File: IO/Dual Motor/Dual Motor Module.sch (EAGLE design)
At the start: 17 parts, among them U1 PCA9685, U2 DRV8837, U3 DRV8837, U7 TPS62142

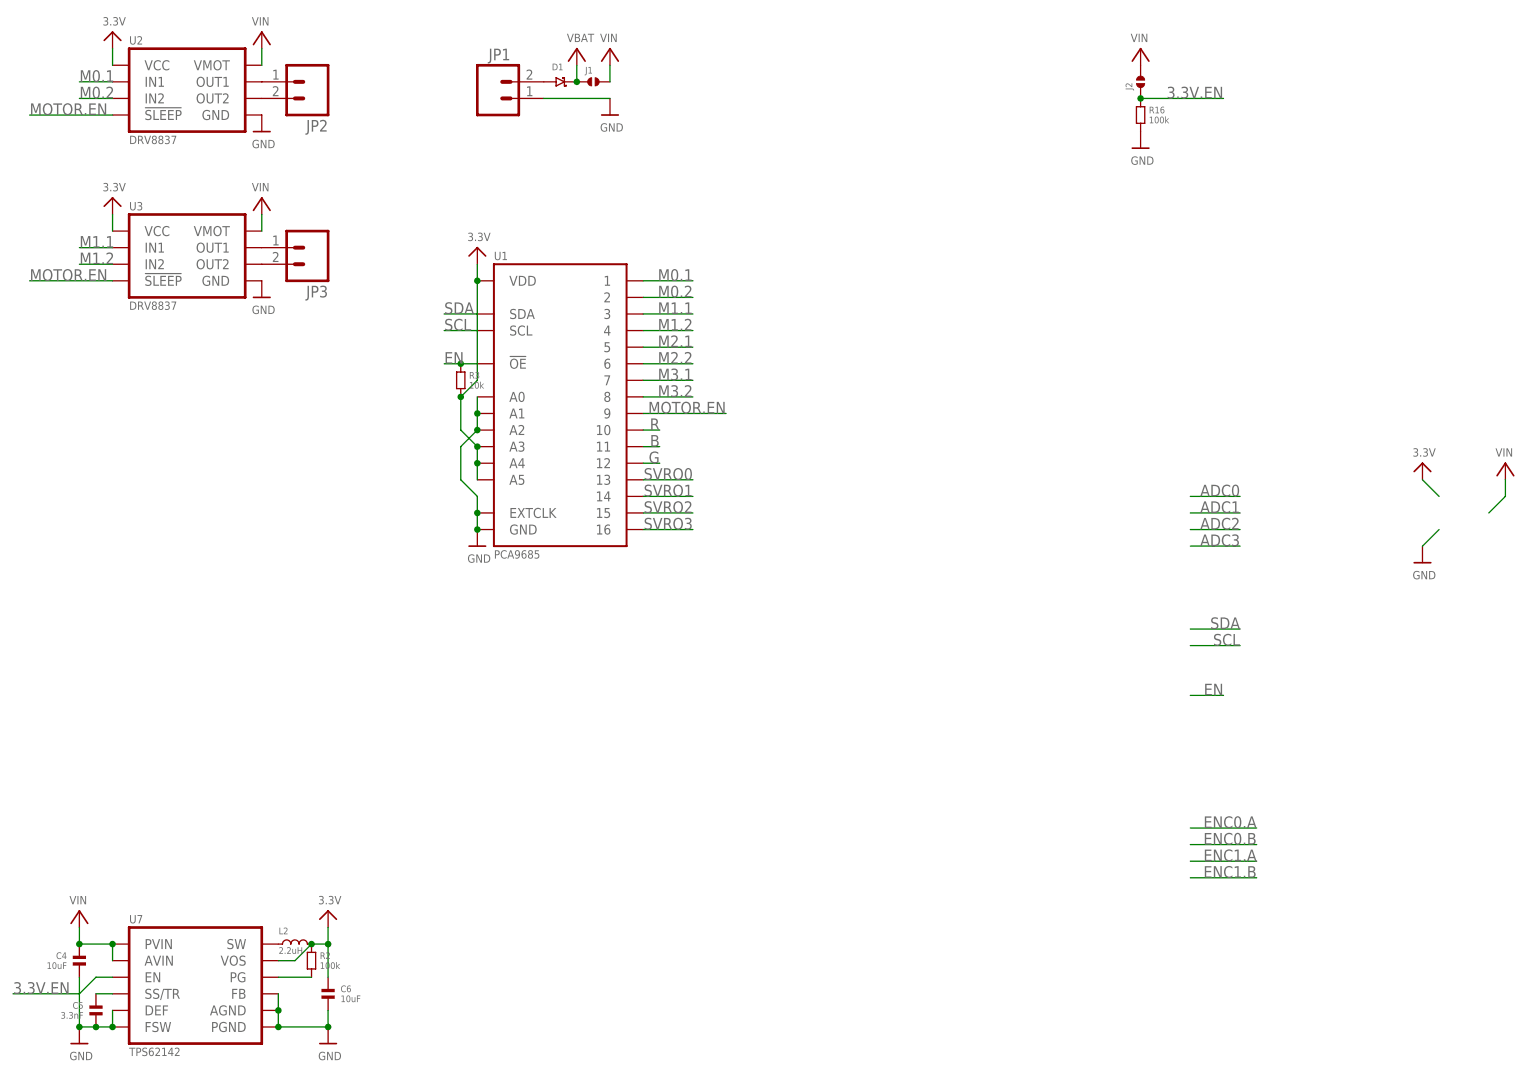
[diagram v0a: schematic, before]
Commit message: Created Dual Motor Module. Schematic complete, components laid out, routing still needed.
Signed-off-by: Cruz Monrreal II <Cruz.Monrreal@gmail.com>
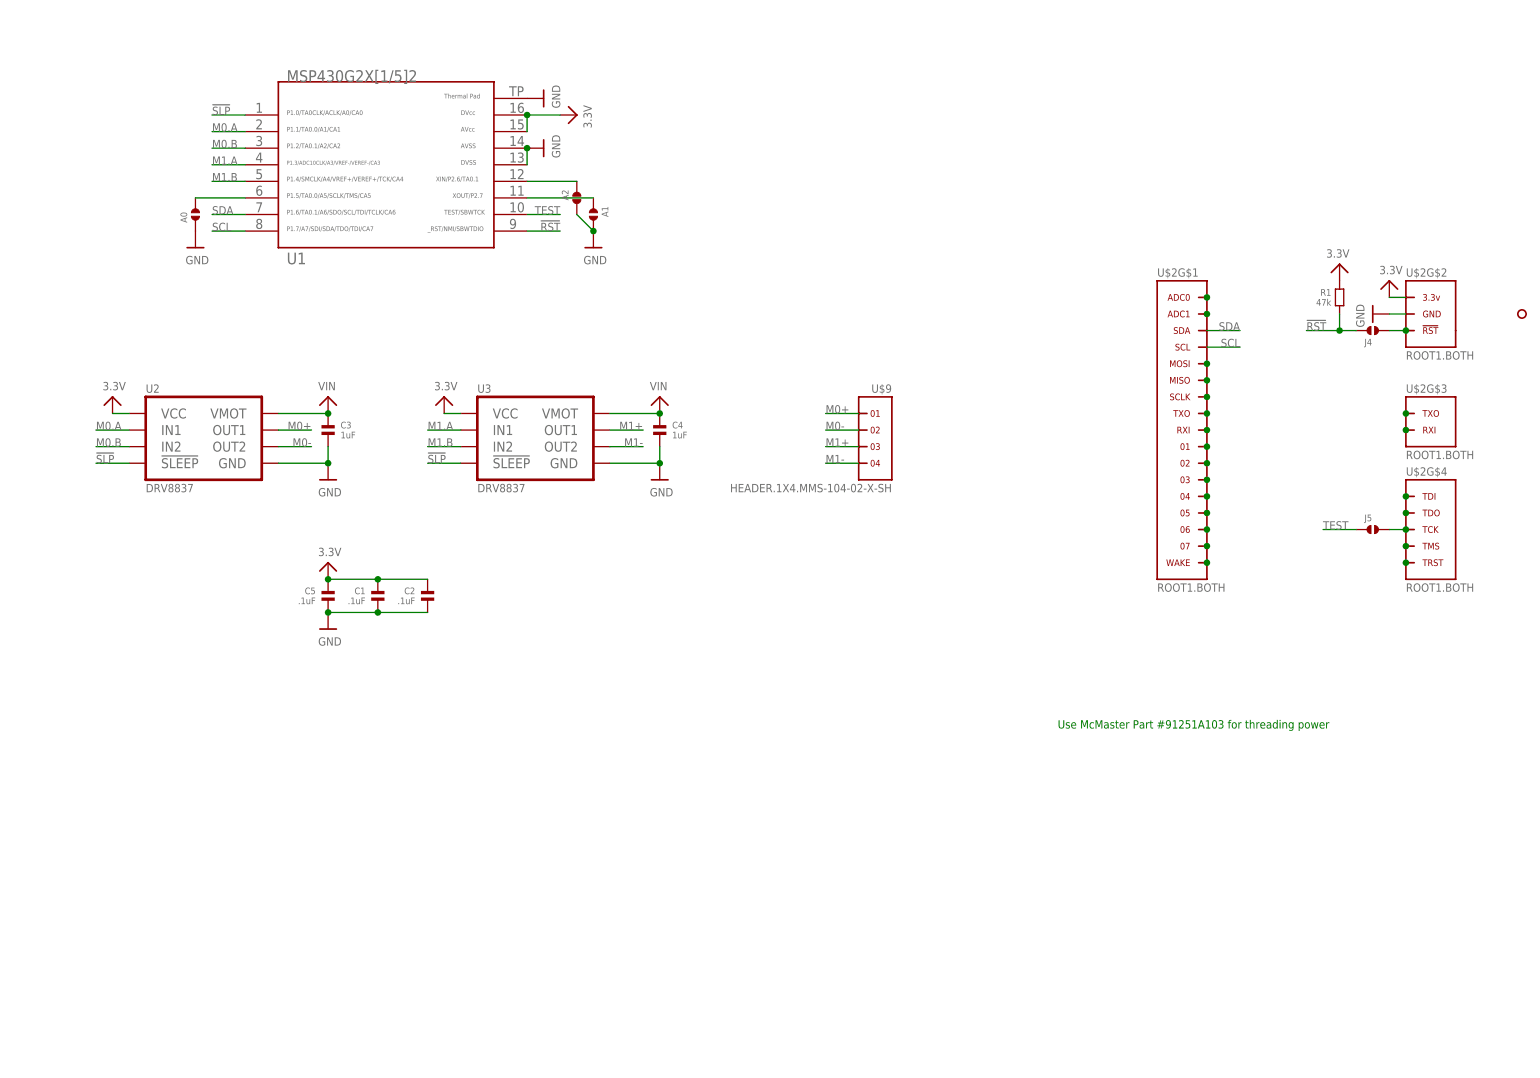
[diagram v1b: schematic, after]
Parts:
- removed C6: 10uF, .standardparts:CAPACITOR.0805
- removed D1: (no value), nxp:DIODE[SCHOTKY]-SOD123W
- removed J1: (no value), .solderjumper:SOLDERJUMPER.2.XL
- removed J2: (no value), .solderjumper:SOLDERJUMPER.2.LRG.PASTE
- removed JP1, JP2, JP3: (no value), SparkFun:M023.5MM
- removed L2: 2.2uH, bourns:INDUCTOR-SRP4020
- removed R16, R2: 100k, .standardparts:RESISTOR.0603
- removed R3: 10k, .standardparts:RESISTOR.0603
- removed U7: TPS62142, .packages(ti):TPS6214X
- added A0, A1, A2, J4, J5: (no value), .solderjumper:SOLDERJUMPER.2.MED
- added C1, C2: .1uF, .standardparts:CAPACITOR.0603
- added C3: 1uF, .standardparts:CAPACITOR.0603
- added R1: 47k, .standardparts:RESISTOR.0603
- added U$2: ROOT1.BOTH, thinkmaketest:ROOT1.BOTH
- added U$4: HOLE.#2, .screw_holes:HOLE.#2
- added U$9: HEADER.1X4.MMS-104-02-X-SH, samtec:HEADER.1X4.MMS-104-02-X-SH
- C4: value 10uF -> 1uF; device .standardparts:CAPACITOR.0805 -> .standardparts:CAPACITOR.0603
- C5: value 3.3nF -> .1uF
- U1: value PCA9685 -> MSP430G2452.QFN16; device nxp:PCA9685 -> TI_MSP430_v16:G2X[1/5]2---RSA16
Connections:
- removed net 3.3V.EN: J2.1, R16.1, U7.EN
- removed net B: U1.11
- removed net EN: R3.1, U1.!OE
- removed net G: U1.12
- removed net M0.1: U1.1, U2.IN1
- removed net M0.2: U1.2, U2.IN2
- removed net M1.1: U1.3, U3.IN1
- removed net M1.2: U1.4, U3.IN2
- removed net M2.1: U1.5
- removed net M2.2: U1.6
- removed net M3.1: U1.7
- removed net M3.2: U1.8
- removed net MOTOR.EN: U1.9, U2.!SLEEP, U3.!SLEEP
- removed net R: U1.10
- removed net SVRO0: U1.13
- removed net SVRO1: U1.14
- removed net SVRO2: U1.15
- removed net SVRO3: U1.16
- removed net VBAT: D1.2, J1.1
- new net !RST: J4.1, R1.2, U1.9
- new net !SLP: U1.1, U2.!SLEEP, U3.!SLEEP
- new net M0+: U$9.1, U2.OUT1
- new net M0-: U$9.2, U2.OUT2
- new net M0.A: U1.2, U2.IN1
- new net M0.B: U1.3, U2.IN2
- new net M1+: U$9.3, U3.OUT1
- new net M1-: U$9.4, U3.OUT2
- new net M1.A: U1.4, U3.IN1
- new net M1.B: U1.5, U3.IN2
- new net N$10: U$2G$1.01
- new net N$11: U$2G$1.02
- new net N$13: U$2G$1.ADC0
- new net N$16: U$2G$1.07
- new net N$17: U$2G$1.WAKE
- new net N$18: U$2G$4.TDI
- new net N$19: U$2G$4.TDO
- new net N$20: J5.2, U$2G$4.TCK
- new net N$21: U$2G$4.TMS
- new net N$22: U$2G$4.TRST
- new net N$23: U$2G$3.RXI
- new net N$24: U$2G$3.TXO
- new net N$25: J4.2, U$2G$2.!RST
- new net N$26: A2.1, U1.12
- new net N$3: A0.2, U1.6
- new net N$5: U$2G$1.03
- new net N$8: U$2G$1.TXO
- new net N$9: U$2G$1.RXI
- new net TEST: J5.1, U1.10
- net 3.3V: now also C1.1, C2.1, C5.1, R1.1, U$2G$2.3.3V, U1.15, U1.16; no longer C6.1, L2.2, R2.1, R3.2, U1.A3, U1.A4, U1.A5, U1.VDD, U7.VOS
- net GND: now also A0.1, A1.2, A2.2, C1.2, C2.2, C3.2, U$2G$2.GND, U1.13, U1.14, U1.TP; no longer C6.2, JP1.1, R16.2, U1.A0, U1.A1, U1.A2, U1.EXTCLK, U1.GND, U7.AGND, U7.DEF, U7.FB, U7.FSW, U7.PGND
- net N$1: now also U$2G$1.04; no longer JP2.1, U2.OUT1
- net N$12: now also U$2G$1.MOSI; no longer L2.1, U7.SW
- net N$14: now also U$2G$1.05; no longer R2.2, U7.PG
- net N$15: now also U$2G$1.06; no longer C5.1, U7.SS/TR
- net N$2: now also U$2G$1.ADC1; no longer D1.1, JP1.2
- net N$4: now also A1.1, U1.11; no longer JP2.2, U2.OUT2
- net N$6: now also U$2G$1.MISO; no longer JP3.1, U3.OUT1
- net N$7: now also U$2G$1.SCLK; no longer JP3.2, U3.OUT2
- net SCL: now also U$2G$1.SCL, U1.8; no longer U1.SCL
- net SDA: now also U$2G$1.SDA, U1.7; no longer U1.SDA
- net VIN: now also C3.1; no longer J1.2, J2.2, U7.AVIN, U7.PVIN
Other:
- note added: "Use McMaster Part #91251A103 for threading power"
- moved on the sheet: C4, C5, U2, U3

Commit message: Updated silkscreen on Dual Motor Module
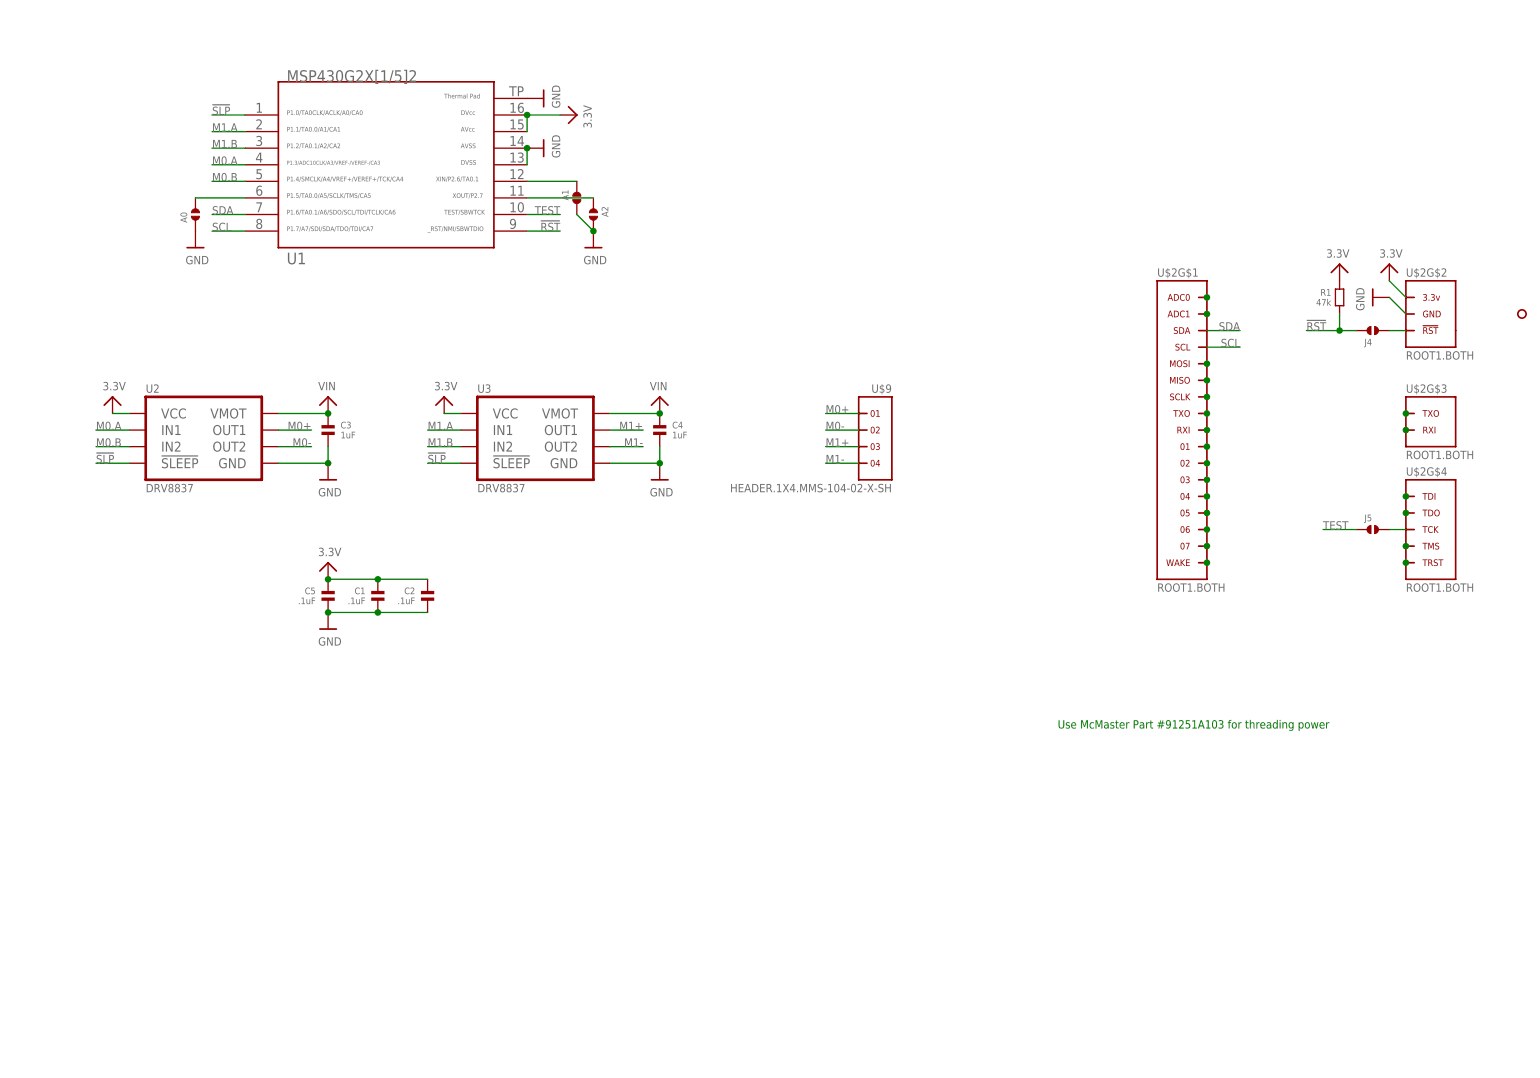
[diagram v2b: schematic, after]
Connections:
- net M0.A: now also U1.4; no longer U1.2
- net M0.B: now also U1.5; no longer U1.3
- net M1.A: now also U1.2; no longer U1.4
- net M1.B: now also U1.3; no longer U1.5
- net N$26: now also A1.1; no longer A2.1
- net N$4: now also A2.1; no longer A1.1
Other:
- moved on the sheet: A1, A2
